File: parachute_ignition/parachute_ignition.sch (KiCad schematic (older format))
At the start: 9 parts, among them P1 CONN_01X02, Q1 IRF7456PBF, U1 LM555N, U2 74LS14

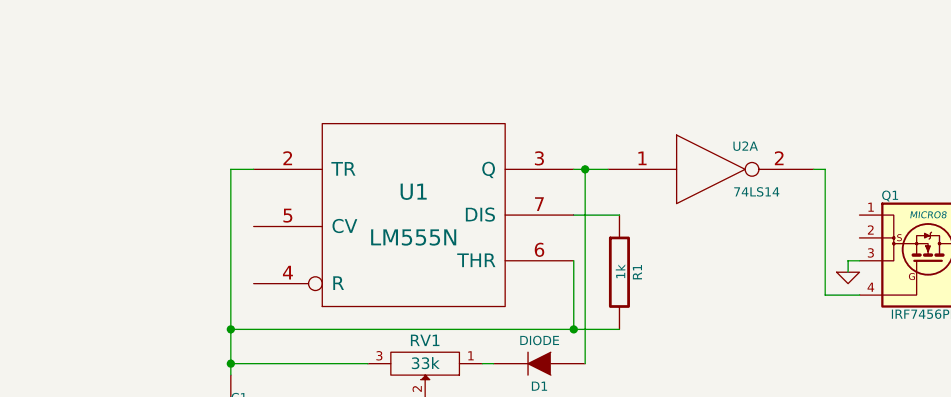
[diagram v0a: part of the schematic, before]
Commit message: power on after jumper disconnection on startup
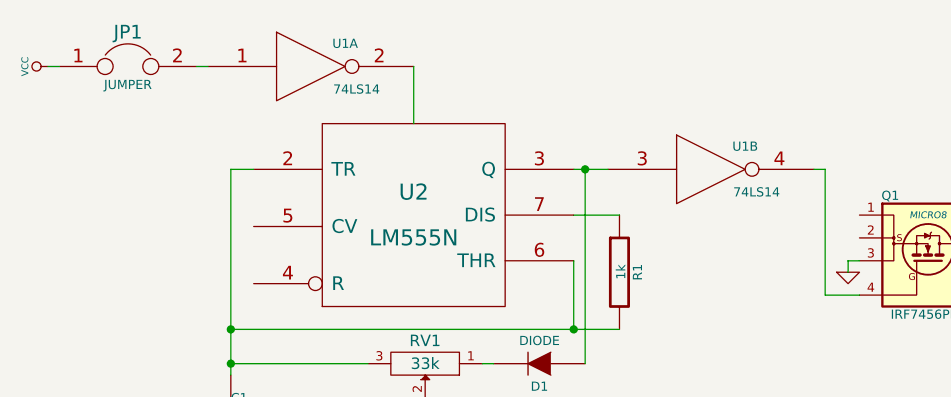
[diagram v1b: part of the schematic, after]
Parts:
- added JP1: JUMPER, symbol JUMPER
- added unit 1 of U1
- renumbered U2 to U1, U1 to U2
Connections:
- net GND: now also U1.7 (GND)
- net VCC: now also JP1.1, U1.14 (VCC), U1.2
- net at D1.1 (A), U2.3 (Q): now also U1.3; no longer U1.1
- net at Q1.4 (G): now also U1.4; no longer U1.2
- new net: JP1.2, U1.1
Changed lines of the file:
@@
 $EndDescr
 $Comp
-L LM555N U1
+L LM555N U2
 U 1 1 5415C6FB
 P 5250 2850
-F 0 "U1" H 5250 2950 70  0000 C CNN
+F 0 "U2" H 5250 2950 70  0000 C CNN
 F 1 "LM555N" H 5250 2750 70  0000 C CNN
 F 2 "" H 5250 2850 60  0000 C CNN
@@
 $EndComp
 $Comp
-L 74LS14 U2
-U 1 1 5415C756
+L 74LS14 U1
+U 2 1 5415C756
 P 6550 2650
-F 0 "U2" H 6700 2750 40  0000 C CNN
+F 0 "U1" H 6700 2750 40  0000 C CNN
 F 1 "74LS14" H 6750 2550 40  0000 C CNN
 F 2 "" H 6550 2650 60  0000 C CNN
 F 3 "" H 6550 2650 60  0000 C CNN
-	1    6550 2650
+	2    6550 2650
 	1    0    0    -1
 $EndComp
@@
 $EndComp
 $Comp
-L VCC #PWR4
+L VCC #PWR01
 U 1 1 5415C86E
 P 8950 2550
-F 0 "#PWR4" H 8950 2650 30  0001 C CNN
+F 0 "#PWR01" H 8950 2650 30  0001 C CNN
 F 1 "VCC" H 8950 2650 30  0000 C CNN
 F 2 "" H 8950 2550 60  0000 C CNN
@@
 $EndComp
 $Comp
-L GND #PWR5
+L GND #PWR02
 U 1 1 5415C882
 P 8950 3250
-F 0 "#PWR5" H 8950 3250 30  0001 C CNN
+F 0 "#PWR02" H 8950 3250 30  0001 C CNN
 F 1 "GND" H 8950 3180 30  0001 C CNN
 F 2 "" H 8950 3250 60  0000 C CNN
@@
 Connection ~ 5950 3350
 $Comp
-L GND #PWR1
+L GND #PWR03
 U 1 1 5415D5B2
 P 4450 4000
-F 0 "#PWR1" H 4450 4000 30  0001 C CNN
+F 0 "#PWR03" H 4450 4000 30  0001 C CNN
 F 1 "GND" H 4450 3930 30  0001 C CNN
 F 2 "" H 4450 4000 60  0000 C CNN
@@
 	7050 3200 7200 3200
 $Comp
-L GND #PWR2
+L GND #PWR04
 U 1 1 5415E7A3
 P 7150 3100
-F 0 "#PWR2" H 7150 3100 30  0001 C CNN
+F 0 "#PWR04" H 7150 3100 30  0001 C CNN
 F 1 "GND" H 7150 3030 30  0001 C CNN
 F 2 "" H 7150 3100 60  0000 C CNN
@@
 	7900 2850 7800 2850
 $Comp
-L VCC #PWR3
+L VCC #PWR05
 U 1 1 5415E821
 P 7850 2750
-F 0 "#PWR3" H 7850 2850 30  0001 C CNN
+F 0 "#PWR05" H 7850 2850 30  0001 C CNN
 F 1 "VCC" H 7850 2850 30  0000 C CNN
 F 2 "" H 7850 2750 60  0000 C CNN
@@
 Wire Wire Line
 	7150 3050 7150 3100
+$Comp
+L 74LS14 U1
+U 1 1 5419CF5C
+P 4800 2200
+F 0 "U1" H 4950 2300 40  0000 C CNN
+F 1 "74LS14" H 5000 2100 40  0000 C CNN
+F 2 "" H 4800 2200 60  0000 C CNN
+F 3 "" H 4800 2200 60  0000 C CNN
+	1    4800 2200
+	1    0    0    -1
+$EndComp
+$Comp
+L JUMPER JP1
+U 1 1 5419D2C4
+P 4000 2200
+F 0 "JP1" H 4000 2350 60  0000 C CNN
+F 1 "JUMPER" H 4000 2120 40  0000 C CNN
+F 2 "" H 4000 2200 60  0000 C CNN
+F 3 "" H 4000 2200 60  0000 C CNN
+	1    4000 2200
+	1    0    0    -1
+$EndComp
+Wire Wire Line
+	4350 2200 4300 2200
+$Comp
+L VCC #PWR06
+U 1 1 5419D445
+P 3650 2200
+F 0 "#PWR06" H 3650 2300 30  0001 C CNN
+F 1 "VCC" H 3650 2300 30  0000 C CNN
+F 2 "" H 3650 2200 60  0000 C CNN
+F 3 "" H 3650 2200 60  0000 C CNN
+	1    3650 2200
+	0    -1   -1   0
+$EndComp
+Wire Wire Line
+	3700 2200 3650 2200
+Wire Wire Line
+	5250 2200 5250 2450
 $EndSCHEMATC

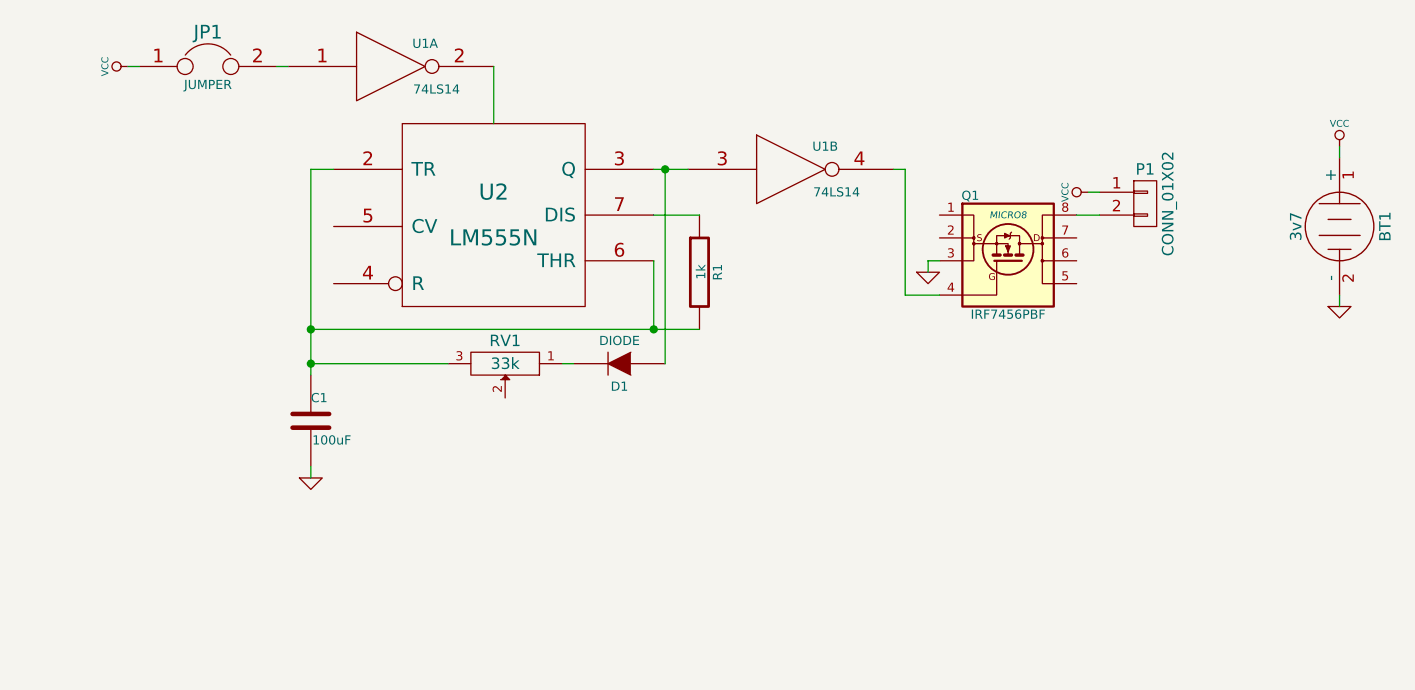
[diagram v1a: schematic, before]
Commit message: 555 and inverter replaced with 4047
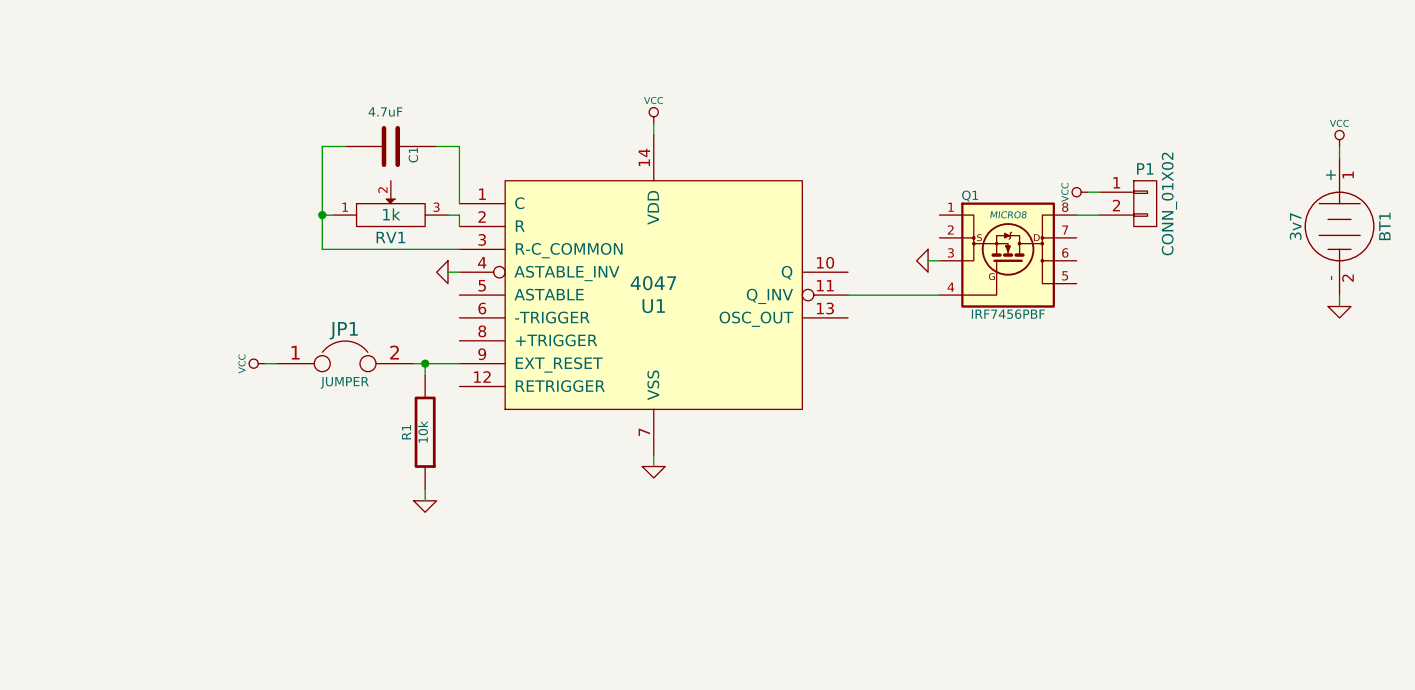
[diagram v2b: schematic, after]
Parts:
- removed D1: DIODE, symbol DIODE
- removed U1: 74LS14, symbol 74LS14
- removed U2: LM555N, symbol LM555N
- added U1: 4047, symbol 4047
- C1: value 100uF -> 4.7uF
- R1: value 1k -> 10k
- RV1: value 33k -> 1k
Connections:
- net GND: now also R1.1, U1.4 (ASTABLE_INV), U1.7 (VSS); no longer C1.2
- net VCC: now also U1.14 (VDD)
- net at Q1.4 (G): now also U1.11 (Q_INV)
- net at RV1.1: now also C1.2, U1.3 (R-C_COMMON)
- net at JP1.2: now also R1.2, U1.9 (EXT_RESET)
- new net: C1.1, U1.1 (C)
- new net: RV1.3, U1.2 (R)
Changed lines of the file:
@@
 EESchema Schematic File Version 2
+LIBS:4047
 LIBS:power
 LIBS:device
@@
 $EndDescr
 $Comp
-L LM555N U2
-U 1 1 5415C6FB
-P 5250 2850
-F 0 "U2" H 5250 2950 70  0000 C CNN
-F 1 "LM555N" H 5250 2750 70  0000 C CNN
-F 2 "" H 5250 2850 60  0000 C CNN
-F 3 "" H 5250 2850 60  0000 C CNN
-	1    5250 2850
-	1    0    0    -1
-$EndComp
-$Comp
-L R R1
-U 1 1 5415C724
-P 6150 3100
-F 0 "R1" V 6230 3100 40  0000 C CNN
-F 1 "1k" V 6157 3101 40  0000 C CNN
-F 2 "" V 6080 3100 30  0000 C CNN
-F 3 "" H 6150 3100 30  0000 C CNN
-	1    6150 3100
-	1    0    0    -1
-$EndComp
-$Comp
-L C C1
-U 1 1 5415C73D
-P 4450 3750
-F 0 "C1" H 4450 3850 40  0000 L CNN
-F 1 "100uF" H 4456 3665 40  0000 L CNN
-F 2 "" H 4488 3600 30  0000 C CNN
-F 3 "" H 4450 3750 60  0000 C CNN
-	1    4450 3750
-	1    0    0    -1
-$EndComp
-$Comp
-L 74LS14 U1
-U 2 1 5415C756
-P 6550 2650
-F 0 "U1" H 6700 2750 40  0000 C CNN
-F 1 "74LS14" H 6750 2550 40  0000 C CNN
-F 2 "" H 6550 2650 60  0000 C CNN
-F 3 "" H 6550 2650 60  0000 C CNN
-	2    6550 2650
-	1    0    0    -1
-$EndComp
-$Comp
 L BATTERY BT1
 U 1 1 5415C7F5
@@
 $EndComp
 $Comp
-L VCC #PWR01
+L VCC #PWR2
 U 1 1 5415C86E
 P 8950 2550
-F 0 "#PWR01" H 8950 2650 30  0001 C CNN
+F 0 "#PWR2" H 8950 2650 30  0001 C CNN
 F 1 "VCC" H 8950 2650 30  0000 C CNN
 F 2 "" H 8950 2550 60  0000 C CNN
@@
 $EndComp
 $Comp
-L GND #PWR02
+L GND #PWR6
 U 1 1 5415C882
 P 8950 3250
-F 0 "#PWR02" H 8950 3250 30  0001 C CNN
+F 0 "#PWR6" H 8950 3250 30  0001 C CNN
 F 1 "GND" H 8950 3180 30  0001 C CNN
 F 2 "" H 8950 3250 60  0000 C CNN
@@
 Wire Wire Line
 	8950 2600 8950 2550
-Wire Wire Line
-	5950 2650 6000 2650
-Wire Wire Line
-	6000 2650 6100 2650
-Wire Wire Line
-	5950 2850 6150 2850
-$Comp
-L DIODE D1
-U 1 1 5415CB96
-P 5800 3500
-F 0 "D1" H 5800 3600 40  0000 C CNN
-F 1 "DIODE" H 5800 3400 40  0000 C CNN
-F 2 "" H 5800 3500 60  0000 C CNN
-F 3 "" H 5800 3500 60  0000 C CNN
-	1    5800 3500
-	-1   0    0    1
-$EndComp
-Connection ~ 6000 2650
-$Comp
-L POT RV1
-U 1 1 5415D089
-P 5300 3500
-F 0 "RV1" H 5300 3400 50  0000 C CNN
-F 1 "33k" H 5300 3500 50  0000 C CNN
-F 2 "" H 5300 3500 60  0000 C CNN
-F 3 "" H 5300 3500 60  0000 C CNN
-	1    5300 3500
-	-1   0    0    1
-$EndComp
-Wire Wire Line
-	5600 3500 5550 3500
-Wire Wire Line
-	5950 3050 5950 3350
-Wire Wire Line
-	4450 3350 5950 3350
-Wire Wire Line
-	5950 3350 6150 3350
-Wire Wire Line
-	4450 2650 4550 2650
-Wire Wire Line
-	6000 3500 6000 2650
-Wire Wire Line
-	4450 3500 5050 3500
-Wire Wire Line
-	4450 2650 4450 3350
-Wire Wire Line
-	4450 3350 4450 3500
-Wire Wire Line
-	4450 3500 4450 3550
-Connection ~ 4450 3500
-Connection ~ 4450 3350
-Connection ~ 5950 3350
-$Comp
-L GND #PWR03
-U 1 1 5415D5B2
-P 4450 4000
-F 0 "#PWR03" H 4450 4000 30  0001 C CNN
-F 1 "GND" H 4450 3930 30  0001 C CNN
-F 2 "" H 4450 4000 60  0000 C CNN
-F 3 "" H 4450 4000 60  0000 C CNN
-	1    4450 4000
-	1    0    0    -1
-$EndComp
-Wire Wire Line
-	4450 3950 4450 4000
 $Comp
 L IRF7607PBF Q1
@@
 	1    0    0    -1
 $EndComp
-Wire Wire Line
-	7000 2650 7050 2650
-Wire Wire Line
-	7050 2650 7050 3200
-Wire Wire Line
-	7050 3200 7200 3200
-$Comp
-L GND #PWR04
+$Comp
+L GND #PWR4
 U 1 1 5415E7A3
-P 7150 3100
-F 0 "#PWR04" H 7150 3100 30  0001 C CNN
-F 1 "GND" H 7150 3030 30  0001 C CNN
-F 2 "" H 7150 3100 60  0000 C CNN
-F 3 "" H 7150 3100 60  0000 C CNN
-	1    7150 3100
-	1    0    0    -1
+P 7150 3050
+F 0 "#PWR4" H 7150 3050 30  0001 C CNN
+F 1 "GND" H 7150 2980 30  0001 C CNN
+F 2 "" H 7150 3050 60  0000 C CNN
+F 3 "" H 7150 3050 60  0000 C CNN
+	1    7150 3050
+	0    1    1    0
 $EndComp
 $Comp
@@
 	7900 2850 7800 2850
 $Comp
-L VCC #PWR05
+L VCC #PWR3
 U 1 1 5415E821
 P 7850 2750
-F 0 "#PWR05" H 7850 2850 30  0001 C CNN
+F 0 "#PWR3" H 7850 2850 30  0001 C CNN
 F 1 "VCC" H 7850 2850 30  0000 C CNN
 F 2 "" H 7850 2750 60  0000 C CNN
@@
 Wire Wire Line
 	7200 3050 7150 3050
-Wire Wire Line
-	7150 3050 7150 3100
-$Comp
-L 74LS14 U1
-U 1 1 5419CF5C
-P 4800 2200
-F 0 "U1" H 4950 2300 40  0000 C CNN
-F 1 "74LS14" H 5000 2100 40  0000 C CNN
-F 2 "" H 4800 2200 60  0000 C CNN
-F 3 "" H 4800 2200 60  0000 C CNN
-	1    4800 2200
-	1    0    0    -1
+$Comp
+L 4047 U1
+U 1 1 541AA5A9
+P 5950 3200
+F 0 "U1" H 5950 3150 60  0000 C CNN
+F 1 "4047" H 5950 3250 60  0000 C CNN
+F 2 "" H 5950 3200 60  0000 C CNN
+F 3 "" H 5950 3200 60  0000 C CNN
+	1    5950 3200
+	1    0    0    -1
+$EndComp
+Wire Wire Line
+	7200 3200 6800 3200
+$Comp
+L VCC #PWR1
+U 1 1 541AA848
+P 5950 2450
+F 0 "#PWR1" H 5950 2550 30  0001 C CNN
+F 1 "VCC" H 5950 2550 30  0000 C CNN
+F 2 "" H 5950 2450 60  0000 C CNN
+F 3 "" H 5950 2450 60  0000 C CNN
+	1    5950 2450
+	1    0    0    -1
+$EndComp
+$Comp
+L GND #PWR8
+U 1 1 541AA857
+P 5950 3950
+F 0 "#PWR8" H 5950 3950 30  0001 C CNN
+F 1 "GND" H 5950 3880 30  0001 C CNN
+F 2 "" H 5950 3950 60  0000 C CNN
+F 3 "" H 5950 3950 60  0000 C CNN
+	1    5950 3950
+	1    0    0    -1
+$EndComp
+Wire Wire Line
+	5950 3900 5950 3950
+Wire Wire Line
+	5950 2500 5950 2450
+$Comp
+L C C1
+U 1 1 541AA8D3
+P 4800 2550
+F 0 "C1" H 4800 2650 40  0000 L CNN
+F 1 "4.7uF" V 4650 2450 40  0000 L CNN
+F 2 "" H 4838 2400 30  0000 C CNN
+F 3 "" H 4800 2550 60  0000 C CNN
+	1    4800 2550
+	0    1    1    0
+$EndComp
+$Comp
+L POT RV1
+U 1 1 541AA977
+P 4800 2850
+F 0 "RV1" H 4800 2750 50  0000 C CNN
+F 1 "1k" H 4800 2850 50  0000 C CNN
+F 2 "" H 4800 2850 60  0000 C CNN
+F 3 "" H 4800 2850 60  0000 C CNN
+	1    4800 2850
+	1    0    0    -1
+$EndComp
+Wire Wire Line
+	5100 2800 5100 2550
+Wire Wire Line
+	5100 2550 5000 2550
+Wire Wire Line
+	4600 2550 4500 2550
+Wire Wire Line
+	4500 2550 4500 3000
+Wire Wire Line
+	4500 3000 5100 3000
+Wire Wire Line
+	4550 2850 4500 2850
+Connection ~ 4500 2850
+$Comp
+L GND #PWR5
+U 1 1 541AAA55
+P 5050 3100
+F 0 "#PWR5" H 5050 3100 30  0001 C CNN
+F 1 "GND" H 5050 3030 30  0001 C CNN
+F 2 "" H 5050 3100 60  0000 C CNN
+F 3 "" H 5050 3100 60  0000 C CNN
+	1    5050 3100
+	0    1    1    0
+$EndComp
+Wire Wire Line
+	5100 3100 5050 3100
+Wire Wire Line
+	5100 2900 5100 2850
+Wire Wire Line
+	5100 2850 5050 2850
+$Comp
+L R R1
+U 1 1 541AACEC
+P 4950 3800
+F 0 "R1" V 5030 3800 40  0000 C CNN
+F 1 "10k" V 4957 3801 40  0000 C CNN
+F 2 "" V 4880 3800 30  0000 C CNN
+F 3 "" H 4950 3800 30  0000 C CNN
+	1    4950 3800
+	-1   0    0    1
 $EndComp
 $Comp
 L JUMPER JP1
-U 1 1 5419D2C4
-P 4000 2200
-F 0 "JP1" H 4000 2350 60  0000 C CNN
-F 1 "JUMPER" H 4000 2120 40  0000 C CNN
-F 2 "" H 4000 2200 60  0000 C CNN
-F 3 "" H 4000 2200 60  0000 C CNN
-	1    4000 2200
-	1    0    0    -1
-$EndComp
-Wire Wire Line
-	4350 2200 4300 2200
-$Comp
-L VCC #PWR06
-U 1 1 5419D445
-P 3650 2200
-F 0 "#PWR06" H 3650 2300 30  0001 C CNN
-F 1 "VCC" H 3650 2300 30  0000 C CNN
-F 2 "" H 3650 2200 60  0000 C CNN
-F 3 "" H 3650 2200 60  0000 C CNN
-	1    3650 2200
+U 1 1 541AAD78
+P 4600 3500
+F 0 "JP1" H 4600 3650 60  0000 C CNN
+F 1 "JUMPER" H 4600 3420 40  0000 C CNN
+F 2 "" H 4600 3500 60  0000 C CNN
+F 3 "" H 4600 3500 60  0000 C CNN
+	1    4600 3500
+	1    0    0    -1
+$EndComp
+Wire Wire Line
+	4900 3500 5100 3500
+Wire Wire Line
+	4950 3550 4950 3500
+Connection ~ 4950 3500
+$Comp
+L VCC #PWR7
+U 1 1 541AAE5F
+P 4250 3500
+F 0 "#PWR7" H 4250 3600 30  0001 C CNN
+F 1 "VCC" H 4250 3600 30  0000 C CNN
+F 2 "" H 4250 3500 60  0000 C CNN
+F 3 "" H 4250 3500 60  0000 C CNN
+	1    4250 3500
 	0    -1   -1   0
 $EndComp
 Wire Wire Line
-	3700 2200 3650 2200
-Wire Wire Line
-	5250 2200 5250 2450
+	4300 3500 4250 3500
+$Comp
+L GND #PWR9
+U 1 1 541AB10D
+P 4950 4100
+F 0 "#PWR9" H 4950 4100 30  0001 C CNN
+F 1 "GND" H 4950 4030 30  0001 C CNN
+F 2 "" H 4950 4100 60  0000 C CNN
+F 3 "" H 4950 4100 60  0000 C CNN
+	1    4950 4100
+	1    0    0    -1
+$EndComp
+Wire Wire Line
+	4950 4100 4950 4050
 $EndSCHEMATC

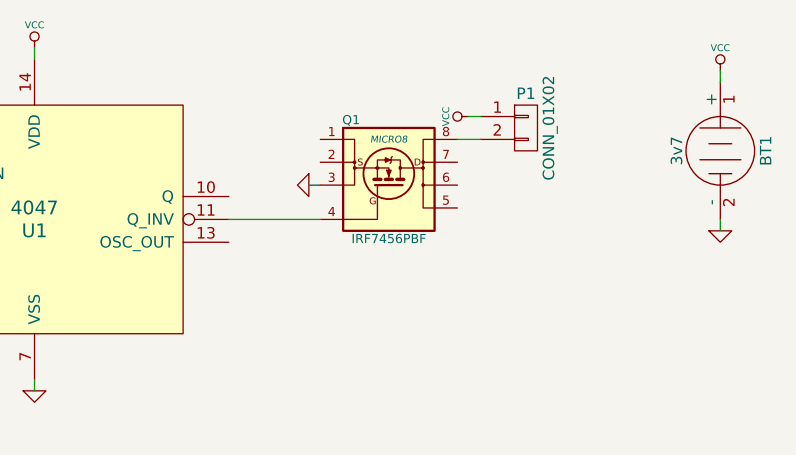
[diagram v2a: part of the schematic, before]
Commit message: different hexfet
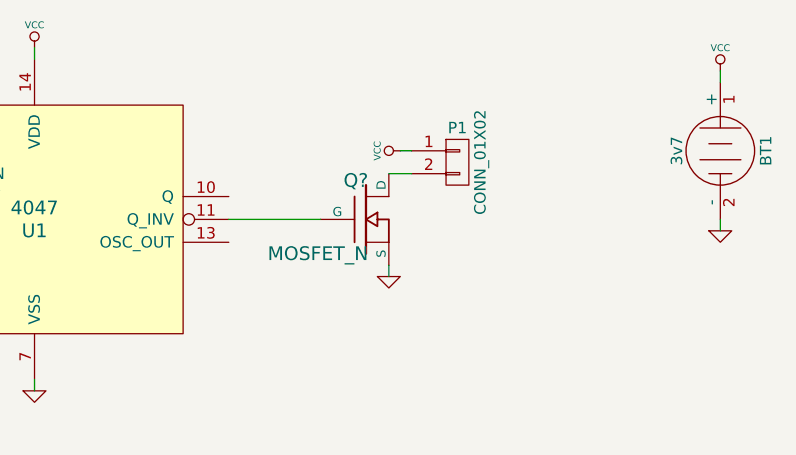
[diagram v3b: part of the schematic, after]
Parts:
- removed Q1: IRF7456PBF, MICRO8, symbol IRF7607PBF
- added Q?: MOSFET_N, symbol MOSFET_N
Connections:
- net GND: now also Q?.S
- net at U1.11 (Q_INV): now also Q?.G
- net at P1.2 (P2): now also Q?.D
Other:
- moved on the sheet: P1
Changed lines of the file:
@@
 	8950 2600 8950 2550
-$Comp
-L IRF7607PBF Q1
-U 1 1 5415E6DB
-P 7500 3050
-F 0 "Q1" H 7335 3335 40  0000 C CNN
-F 1 "IRF7456PBF" H 7500 2815 40  0000 C CNN
-F 2 "MICRO8" H 7500 3250 30  0000 C CIN
-F 3 "" V 7500 3050 60  0000 C CNN
-	1    7500 3050
-	1    0    0    -1
-$EndComp
 $Comp
 L GND #PWR4
 U 1 1 5415E7A3
-P 7150 3050
-F 0 "#PWR4" H 7150 3050 30  0001 C CNN
-F 1 "GND" H 7150 2980 30  0001 C CNN
-F 2 "" H 7150 3050 60  0000 C CNN
-F 3 "" H 7150 3050 60  0000 C CNN
-	1    7150 3050
-	0    1    1    0
+P 7500 3450
+F 0 "#PWR4" H 7500 3450 30  0001 C CNN
+F 1 "GND" H 7500 3380 30  0001 C CNN
+F 2 "" H 7500 3450 60  0000 C CNN
+F 3 "" H 7500 3450 60  0000 C CNN
+	1    7500 3450
+	1    0    0    -1
 $EndComp
 $Comp
 L CONN_01X02 P1
 U 1 1 5415E7CD
-P 8100 2800
-F 0 "P1" H 8100 2950 50  0000 C CNN
-F 1 "CONN_01X02" V 8200 2800 50  0000 C CNN
-F 2 "" H 8100 2800 60  0000 C CNN
-F 3 "" H 8100 2800 60  0000 C CNN
-	1    8100 2800
+P 7800 2950
+F 0 "P1" H 7800 3100 50  0000 C CNN
+F 1 "CONN_01X02" V 7900 2950 50  0000 C CNN
+F 2 "" H 7800 2950 60  0000 C CNN
+F 3 "" H 7800 2950 60  0000 C CNN
+	1    7800 2950
 	1    0    0    -1
 $EndComp
 Wire Wire Line
-	7900 2850 7800 2850
+	7600 3000 7500 3000
 $Comp
 L VCC #PWR3
 U 1 1 5415E821
-P 7850 2750
-F 0 "#PWR3" H 7850 2850 30  0001 C CNN
-F 1 "VCC" H 7850 2850 30  0000 C CNN
-F 2 "" H 7850 2750 60  0000 C CNN
-F 3 "" H 7850 2750 60  0000 C CNN
-	1    7850 2750
+P 7550 2900
+F 0 "#PWR3" H 7550 3000 30  0001 C CNN
+F 1 "VCC" H 7550 3000 30  0000 C CNN
+F 2 "" H 7550 2900 60  0000 C CNN
+F 3 "" H 7550 2900 60  0000 C CNN
+	1    7550 2900
 	0    -1   -1   0
 $EndComp
 Wire Wire Line
-	7900 2750 7850 2750
-Wire Wire Line
-	7200 3050 7150 3050
+	7600 2900 7550 2900
 $Comp
 L 4047 U1
@@
 Wire Wire Line
 	4950 4100 4950 4050
+$Comp
+L MOSFET_N Q?
+U 1 1 541B5102
+P 7400 3200
+F 0 "Q?" H 7410 3370 60  0000 R CNN
+F 1 "MOSFET_N" H 7410 3050 60  0000 R CNN
+F 2 "" H 7400 3200 60  0000 C CNN
+F 3 "" H 7400 3200 60  0000 C CNN
+	1    7400 3200
+	1    0    0    -1
+$EndComp
+Wire Wire Line
+	7500 3450 7500 3400
 $EndSCHEMATC

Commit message: emengercy quicksave
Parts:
- removed Q?: MOSFET_N, symbol MOSFET_N
- added BT1: 3v7, Pin_Headers:Pin_Header_Straight_1x02, symbol BATTERY
- added Q1: IRF7413ZPBF, SMD_Packages:SOIC-8-W, symbol IRF7607PBF
- BT2: renamed from BT1; value 3v7 -> 3v; footprint (none) -> Coin Cell Holder:Coin_Cell_Holder_CH25-2032LF
- C1: value 4.7uF -> 4u7; footprint (none) -> Capacitors_SMD:C_0805
- JP1, P1: footprint (none) -> Pin_Headers:Pin_Header_Straight_1x02
- R1: footprint (none) -> Resistors_SMD:R_0805_HandSoldering
- RV1: footprint (none) -> Koa Trimmer Smd:Koa_Trimmer_Smd_C
- U1: footprint (none) -> SMD_Packages:SOIC-14_W
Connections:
- net VCC: no longer P1.1 (P1)
- net at P1.2 (P2): now also Q1.8 (D)
- net at U1.11 (Q_INV): now also Q1.4 (G)
- new net: BT1.1 (+), P1.1 (P1)
- new net: BT1.2 (-), Q1.3 (S)
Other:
- moved on the sheet: BT2, C1, JP1, P1, R1, RV1, U1
